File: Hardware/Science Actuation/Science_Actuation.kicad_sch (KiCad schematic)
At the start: 111 parts, among them J2 RJ45_LED_Shielded, Q1 BSS138, Q10 AO3401A, Q9 BSS138, SW1 SW_Push, SW10 SW_SPDT, SW2 SW_Push, SW3 SW_Push, SW4 SW_Push, SW5 SW_Push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

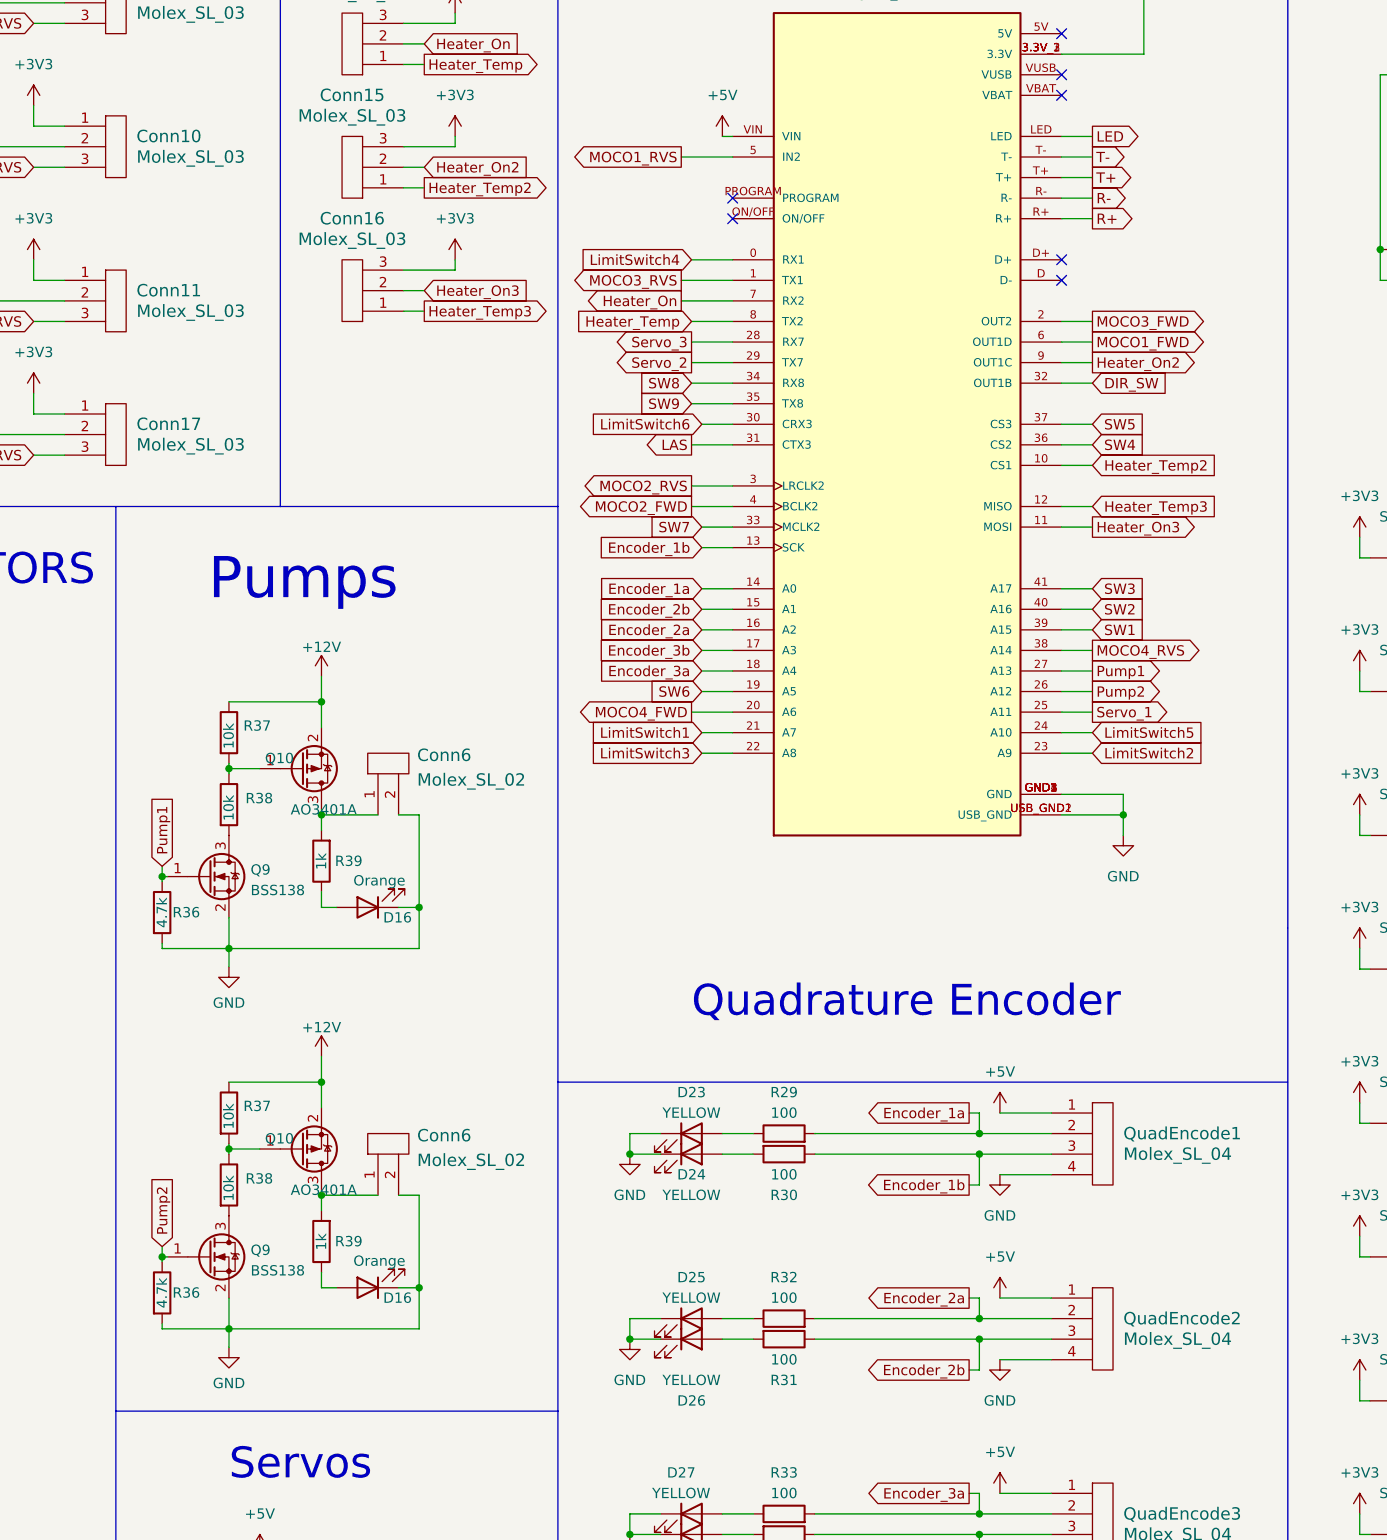
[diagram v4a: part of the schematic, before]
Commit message: Updated Schematic
Cleaned up traces and other miscellaneous things
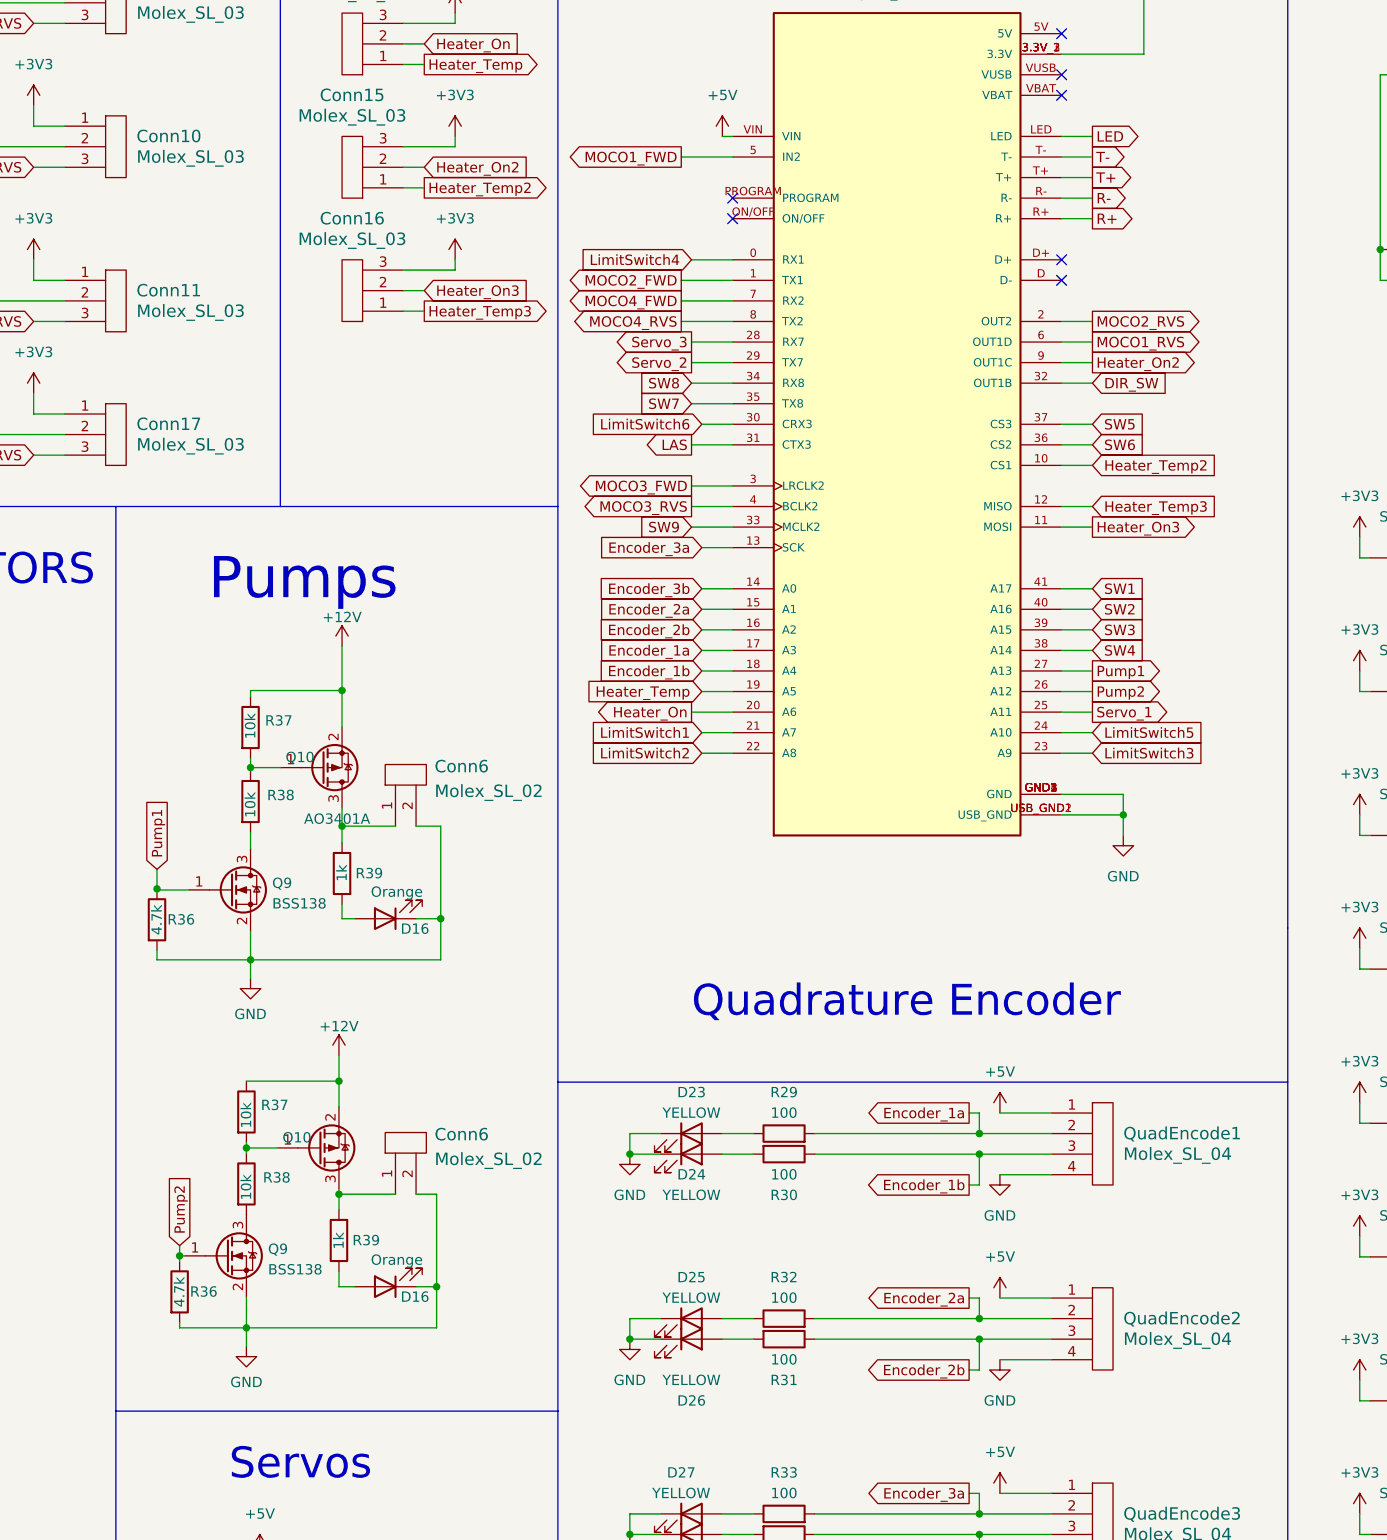
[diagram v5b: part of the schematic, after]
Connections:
- net Encoder_1a: now also U2.17 (A3); no longer U2.14 (A0)
- net Encoder_1b: now also U2.18 (A4); no longer U2.13 (SCK)
- net Encoder_2a: now also U2.15 (A1); no longer U2.16 (A2)
- net Encoder_2b: now also U2.16 (A2); no longer U2.15 (A1)
- net Encoder_3a: now also U2.13 (SCK); no longer U2.18 (A4)
- net Encoder_3b: now also U2.14 (A0); no longer U2.17 (A3)
- net Heater_On: now also U2.20 (A6); no longer U2.7 (RX2)
- net Heater_Temp: now also U2.19 (A5); no longer U2.8 (TX2)
- net LimitSwitch2: now also U2.22 (A8); no longer U2.23 (A9)
- net LimitSwitch3: now also U2.23 (A9); no longer U2.22 (A8)
- net MOCO1_FWD: now also U2.5 (IN2); no longer U2.6 (OUT1D)
- net MOCO1_RVS: now also U2.6 (OUT1D); no longer U2.5 (IN2)
- net MOCO2_FWD: now also U2.1 (TX1); no longer U2.4 (BCLK2)
- net MOCO2_RVS: now also U2.2 (OUT2); no longer U2.3 (LRCLK2)
- net MOCO3_FWD: now also U2.3 (LRCLK2); no longer U2.2 (OUT2)
- net MOCO3_RVS: now also U2.4 (BCLK2); no longer U2.1 (TX1)
- net MOCO4_FWD: now also U2.7 (RX2); no longer U2.20 (A6)
- net MOCO4_RVS: now also U2.8 (TX2); no longer U2.38 (A14)
- net SW1: now also U2.41 (A17); no longer U2.39 (A15)
- net SW3: now also U2.39 (A15); no longer U2.41 (A17)
- net SW4: now also U2.38 (A14); no longer U2.36 (CS2)
- net SW6: now also U2.36 (CS2); no longer U2.19 (A5)
- net SW7: now also U2.35 (TX8); no longer U2.33 (MCLK2)
- net SW9: now also U2.33 (MCLK2); no longer U2.35 (TX8)
- net at Conn6.1, Q10.3 (D): now also R39.1; no longer R39.2
- net at D16.2 (A): now also R39.2; no longer R39.1
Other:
- moved on the sheet: Conn6, D16, Q10, Q9, R36, R37, R38, R39

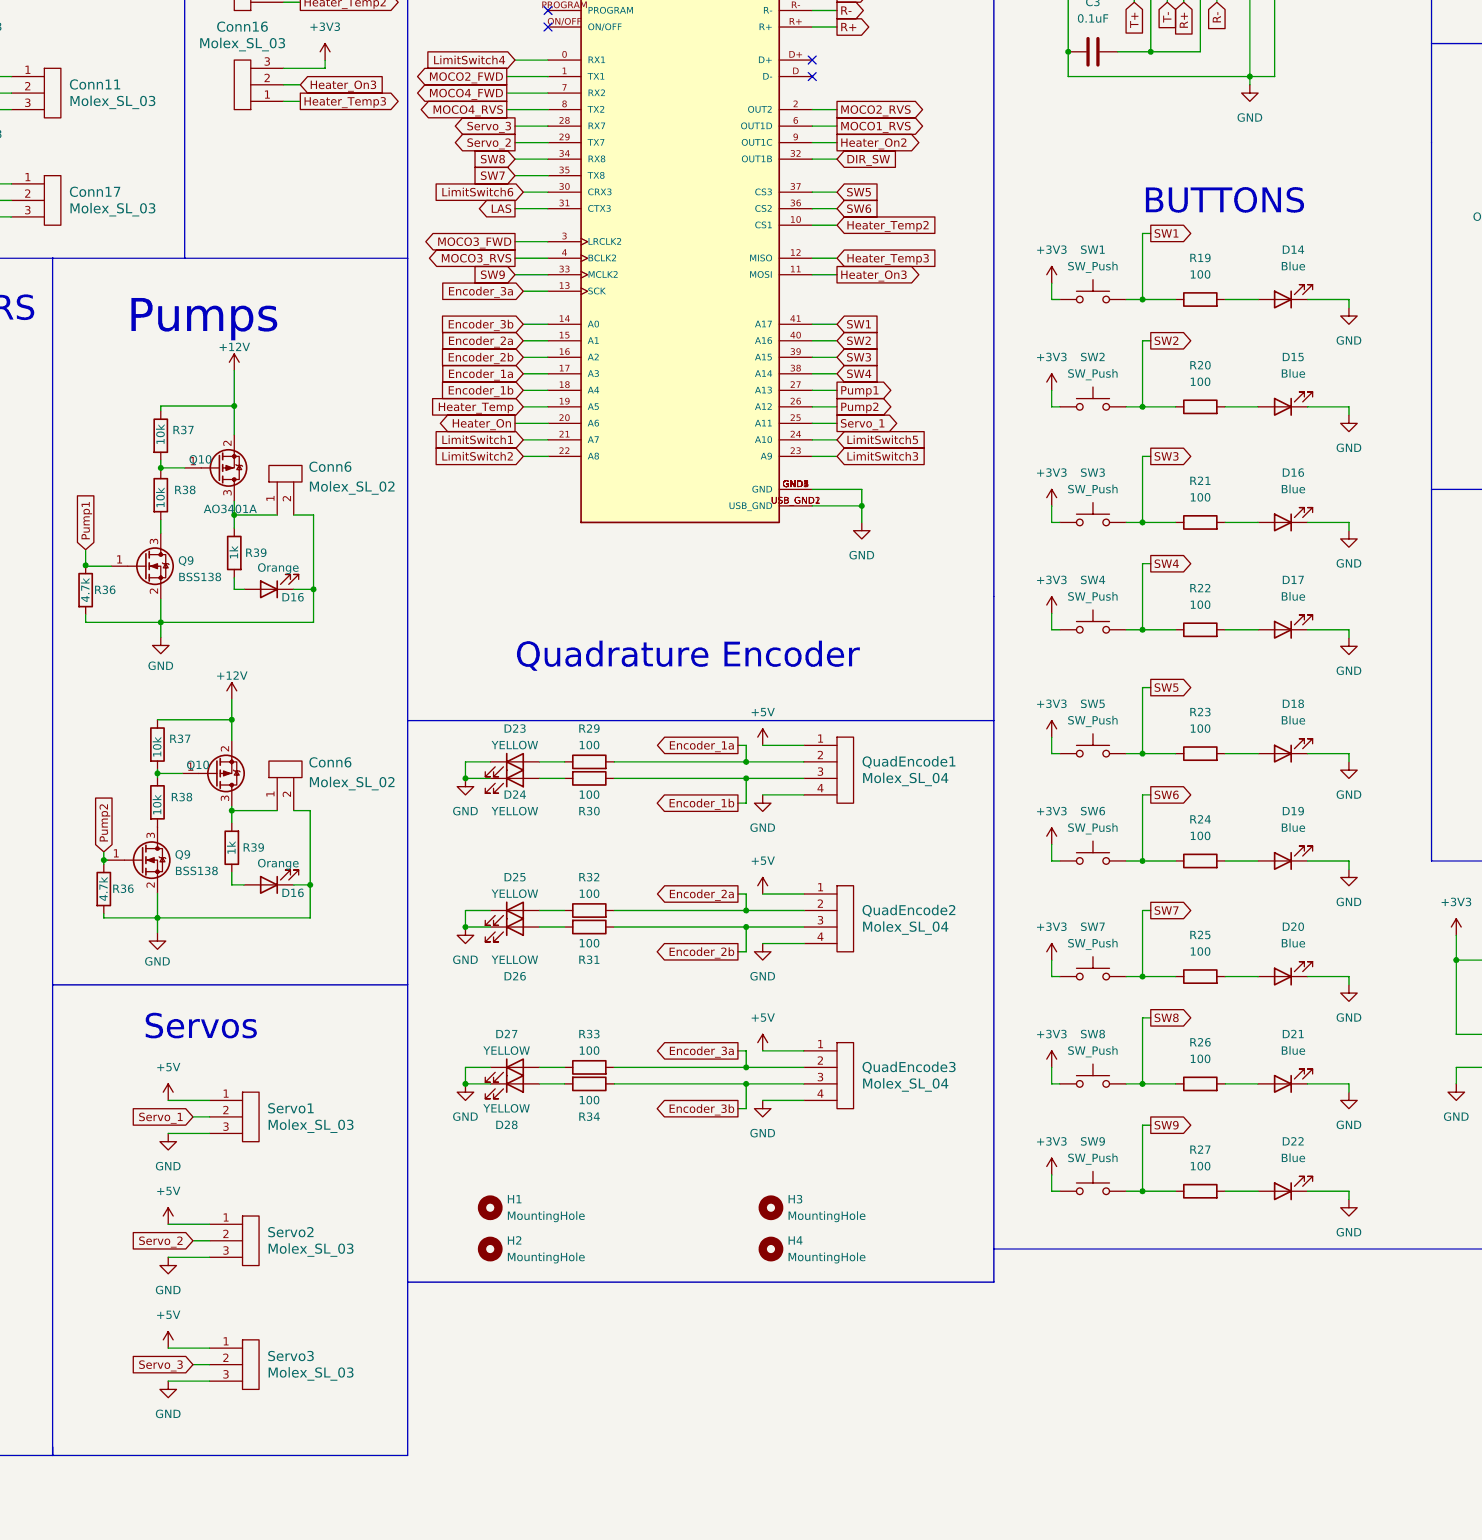
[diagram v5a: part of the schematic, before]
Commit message: Updated Rev1 for parts ordering
Changed 12V and 5V traces, removed servo3, added heater4, updated BOM (may want to doublecheck the BOM), removed SW9, made labels for switches bigger, and hopefully correctly made the GERB
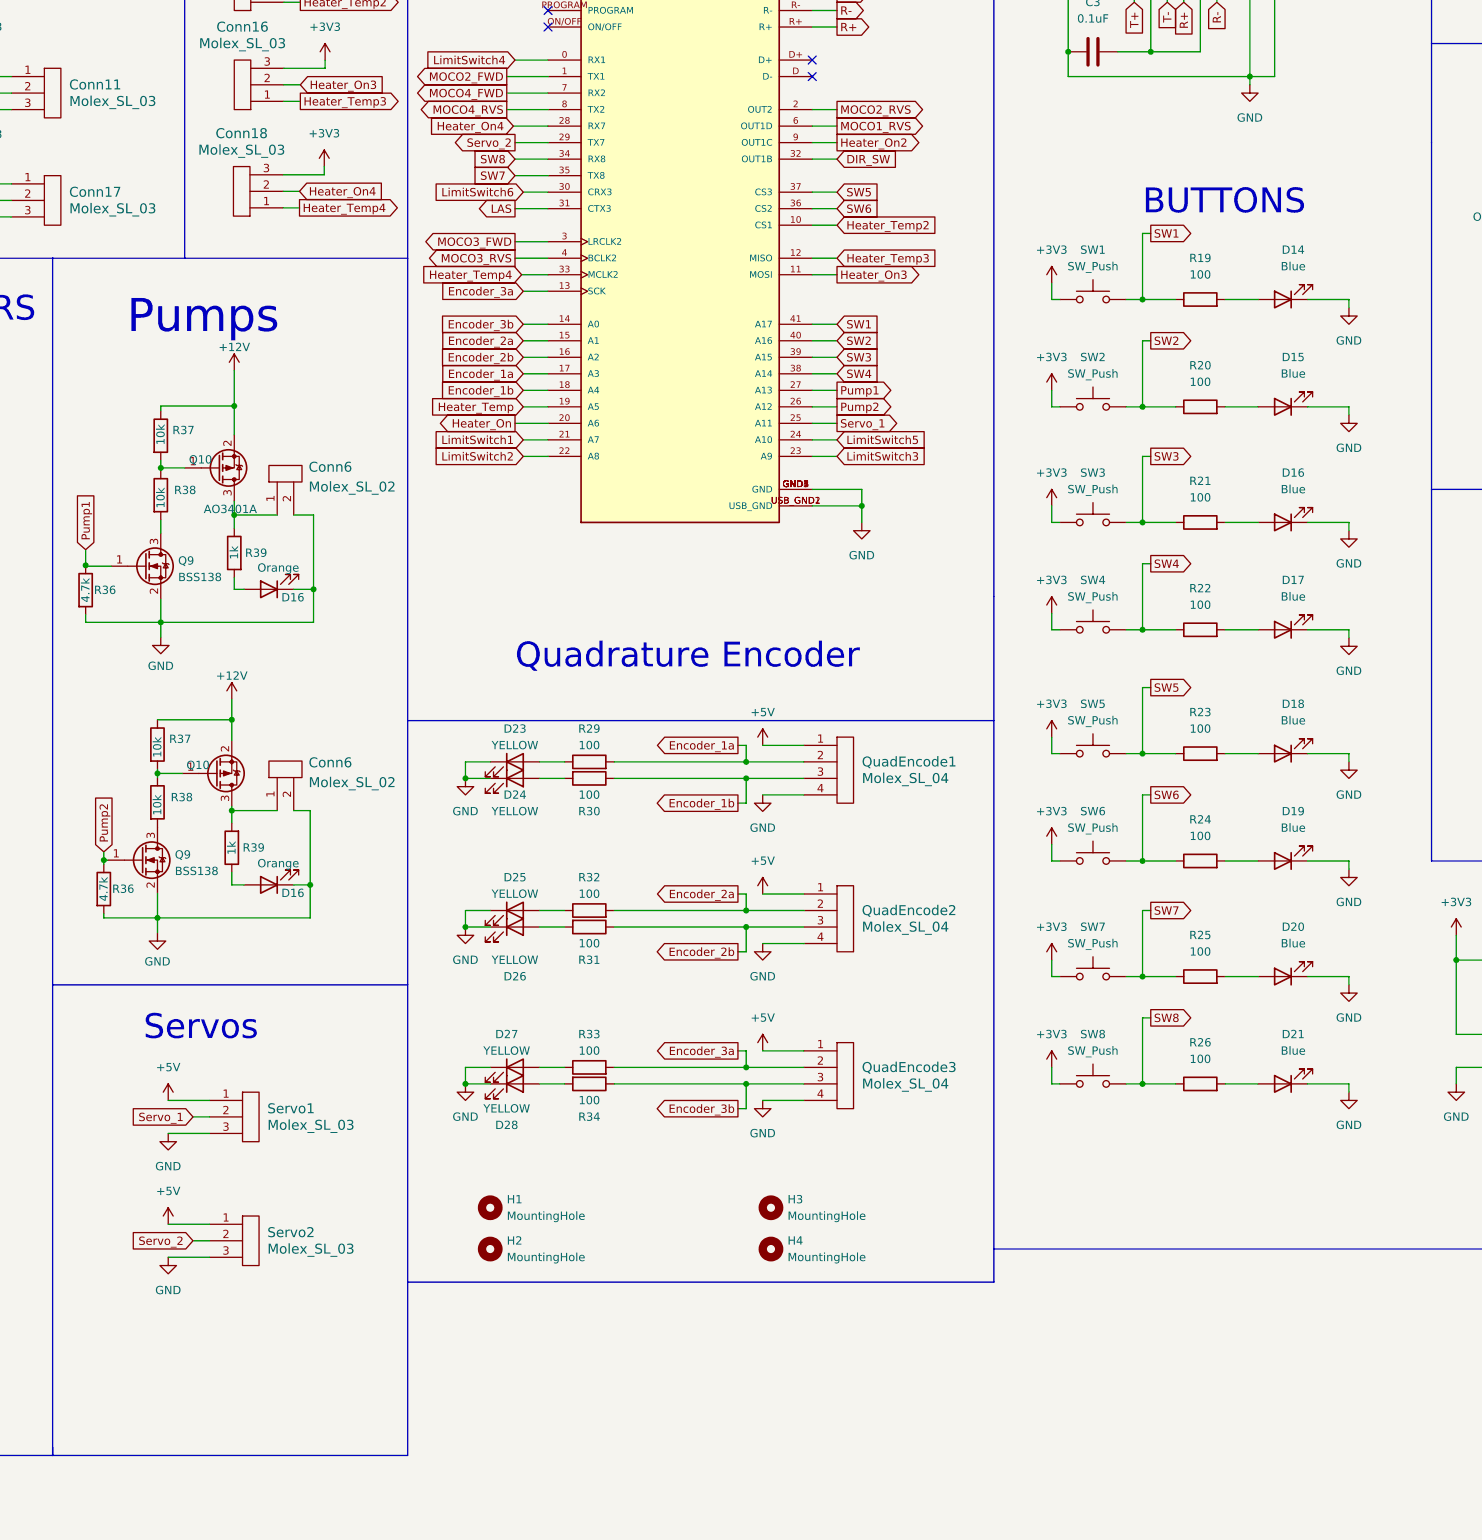
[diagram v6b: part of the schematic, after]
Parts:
- removed D22: Blue, LED_SMD:LED_0603_1608Metric_Pad1.05x0.95mm_HandSolder, symbol Device:LED
- removed R27: 100, Resistor_SMD:R_0603_1608Metric_Pad0.98x0.95mm_HandSolder, symbol Device:R
- removed SW9: SW_Push, Button_Switch_SMD:SW_SPST_TL3305A, symbol Switch:SW_Push
- removed Servo3: Molex_SL_03, MRDT_Connectors:MOLEX_SL_03_Vertical, symbol MRDT_Connectors:Molex_SL_03
- added Conn18: Molex_SL_03, MRDT_Connectors:MOLEX_SL_03_Vertical, symbol MRDT_Connectors:Molex_SL_03
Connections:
- net +3V3: now also Conn18.3
- net SW9 renamed Heater_Temp4
- net Heater_Temp4: now also Conn18.1
- net Servo_3 renamed Heater_On4
- net Heater_On4: now also Conn18.2
